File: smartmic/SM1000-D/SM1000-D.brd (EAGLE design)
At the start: 65 x 100 mm, 198 parts, among them CN1 HDR100-3, CN10 ST-3509, CN11 HDR100-3, CN12 HRS-A3C-16DA, CN2 JS-MU3-002, CN3 DS-0518, CN4 RJ-45, CN5 ST-3509, CN6 ST-3509, CN7 ST-3509, CN8 ST-3509, CN9 ST-3509, J1 JMP-2PIN, J3 JMP-2PIN, J4 JMP-2PIN, P1 TPAD50, P10 TPAD50, P11 TPAD50, P12 TPAD50, P13 TPAD50, P14 TPAD50, P16 TPAD50, P18 TPAD50, P19 TPAD50, P2 TPAD50, P20 TPAD50, P3 TPAD50, P4 TPAD50, P5 TPAD50, P6 TPAD50, P7 TPAD50, P8 TPAD50, P9 TPAD50, SW1 SW-SPDT-8US8WR2C2M7RES, SW2 TS-026, SW3 DPDT, SW4 TS-026, SW5 TS-02B, T1 SM-LP-5001, T2 SM-LP-5001, U1 STM32F405VGT6, U2 LD3985M33R, U3 STMPS2141, U4 EMIF02-USB03F2, U5 TPS54329E, U6 LMV341, U7 LMV341, U8 LM386M-1, U9 LMV341

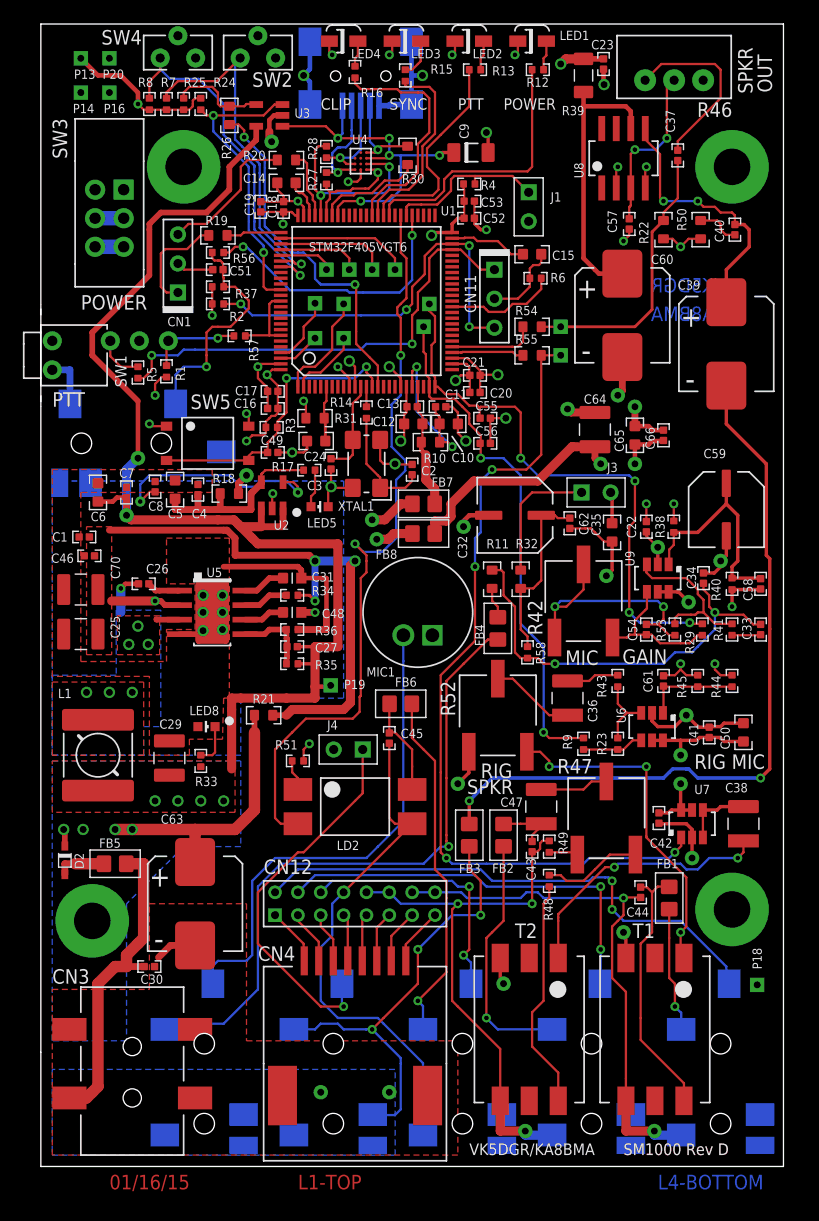
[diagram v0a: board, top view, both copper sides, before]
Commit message: Move Top Assembly items to separate drawing
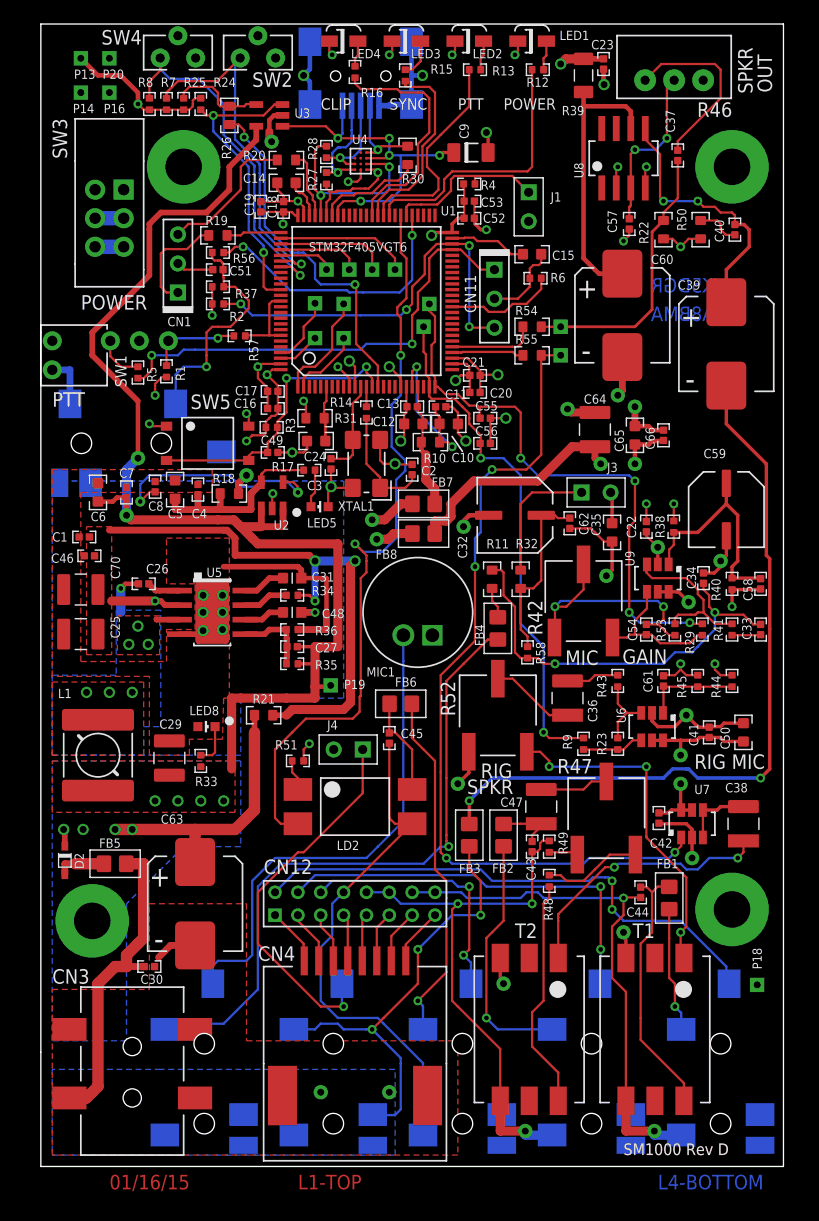
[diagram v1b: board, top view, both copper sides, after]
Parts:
- added CABLE1: CABLE,SPKR 50mm + CONNECTOR, _RoweTel:NOPACKAGE
- added CABLE2: CABLE, USB-A/F TO MICRO USB-A/M, _RoweTel:NOPACKAGE
- added ENCL1: ENCL-SM1000-B-BOTTOM, _RoweTel:NOPACKAGE
- added ENCL2: ENCL-SM1000-B-TOP, _RoweTel:NOPACKAGE
- added ENCL3: ENCL-SM1000-B-SIDE PLATE, _RoweTel:NOPACKAGE
- added HDWE1: SCREW,2-56 X 1/4 X 4, _RoweTel:NOPACKAGE
- added HDWE2: WASHER, 2-56 X 4, _RoweTel:NOPACKAGE
- added HDWE3: NUT, 2-56 X 4, _RoweTel:NOPACKAGE
- added HDWE4: SCREW, SELF TAPPING, 2.2mm x 6mm X 4, _RoweTel:NOPACKAGE
- added HDWE5: JUMPER, 50mm X 4, _RoweTel:NOPACKAGE
- added KNOB1: KNOB, 3.5mm SHAFT, FOR R46, _RoweTel:NOPACKAGE
- added PS1: POWER SUPPLY, 12VDC,500ma, _RoweTel:NOPACKAGE
- added U$5: PRELIMINARY, _RoweTel:NOPACKAGE
- PCB1: value SM1000C -> SM1000D
- R42: value 500K,POT -> 500K,TrimPOT
- R47: value 500,POT -> 500,TrimPOT
- R52: value 1K,POT -> 1K,TrimPOT
- moved SPKR1 78.8 mm to (-43.5, -66.5)
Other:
- board text removed: "VK5DGR/KA8BMA"

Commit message: Production Release of SM1000-D PCB files
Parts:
- removed CABLE1: CABLE,SPKR 50mm + CONNECTOR, _RoweTel:NOPACKAGE
- removed CABLE2: CABLE, USB-A/F TO MICRO USB-A/M, _RoweTel:NOPACKAGE
- removed ENCL1: ENCL-SM1000-B-BOTTOM, _RoweTel:NOPACKAGE
- removed ENCL2: ENCL-SM1000-B-TOP, _RoweTel:NOPACKAGE
- removed ENCL3: ENCL-SM1000-B-SIDE PLATE, _RoweTel:NOPACKAGE
- removed HDWE1: SCREW,2-56 X 1/4 X 4, _RoweTel:NOPACKAGE
- removed HDWE2: WASHER, 2-56 X 4, _RoweTel:NOPACKAGE
- removed HDWE3: NUT, 2-56 X 4, _RoweTel:NOPACKAGE
- removed HDWE4: SCREW, SELF TAPPING, 2.2mm x 6mm X 4, _RoweTel:NOPACKAGE
- removed HDWE5: JUMPER, 50mm X 4, _RoweTel:NOPACKAGE
- removed KNOB1: KNOB, 3.5mm SHAFT, FOR R46, _RoweTel:NOPACKAGE
- removed PS1: POWER SUPPLY, 12VDC,500ma, _RoweTel:NOPACKAGE
- removed U$5: PRELIMINARY, _RoweTel:NOPACKAGE
- moved SPKR1 81.6 mm to (4.50, -0.50)
- moved DRILEGEND 6.71 mm to (21.3, -19.7)
